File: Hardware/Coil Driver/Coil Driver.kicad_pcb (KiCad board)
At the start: 4 copper layers, 50 x 50 mm, 88 parts, among them J1 Barrel_Jack_Switch, J2 0.1" Header, J3 Tag-connect-NL, J4 0.1" Header, Q1 DMN3023L, Q2 DMN3023L, Q3 DMN3023L, Q4 DMN3023L, SW1 BTN_RST, SW2 BTN_USR1, SW3 BTN_USR2, U1 DGD05473, U2 MCP16331, U3 DGD05473, U4 STM32F070F6P6, Y1 8MHz

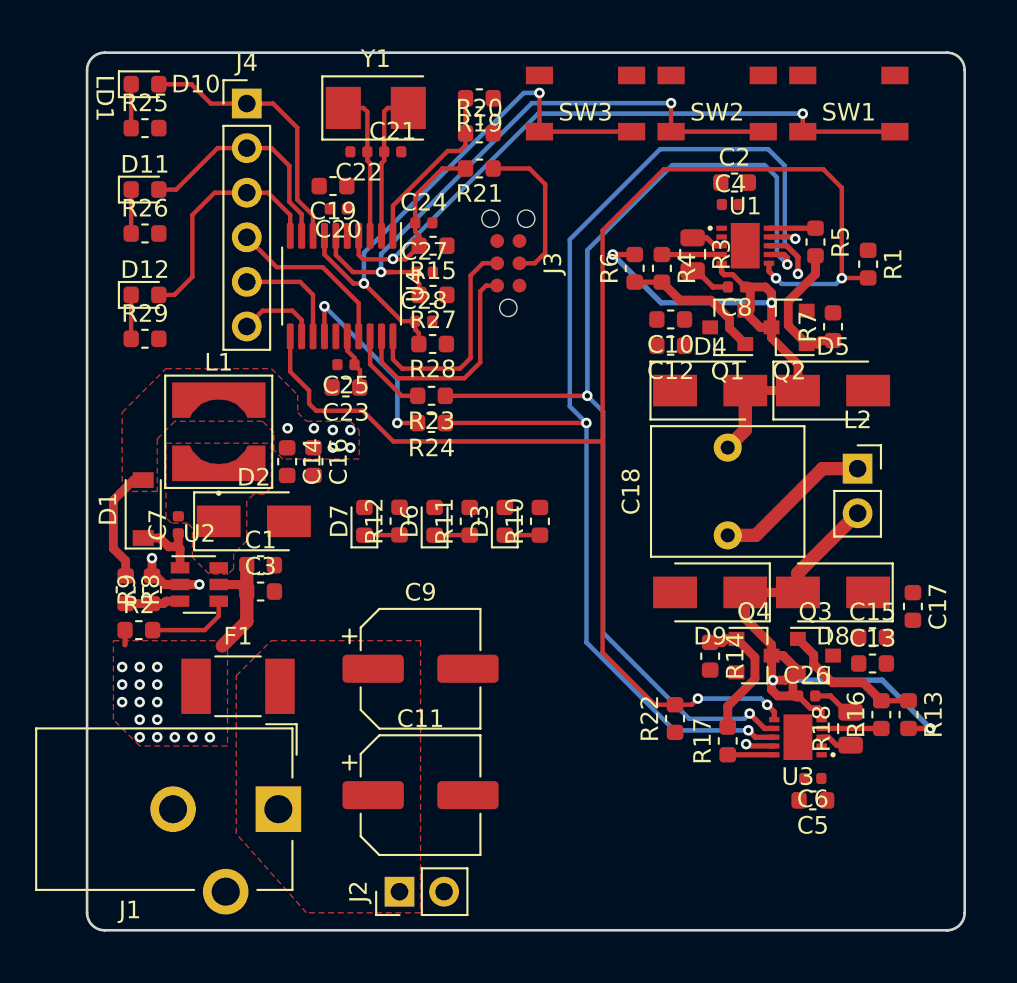
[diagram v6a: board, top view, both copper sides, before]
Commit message: added ground vias
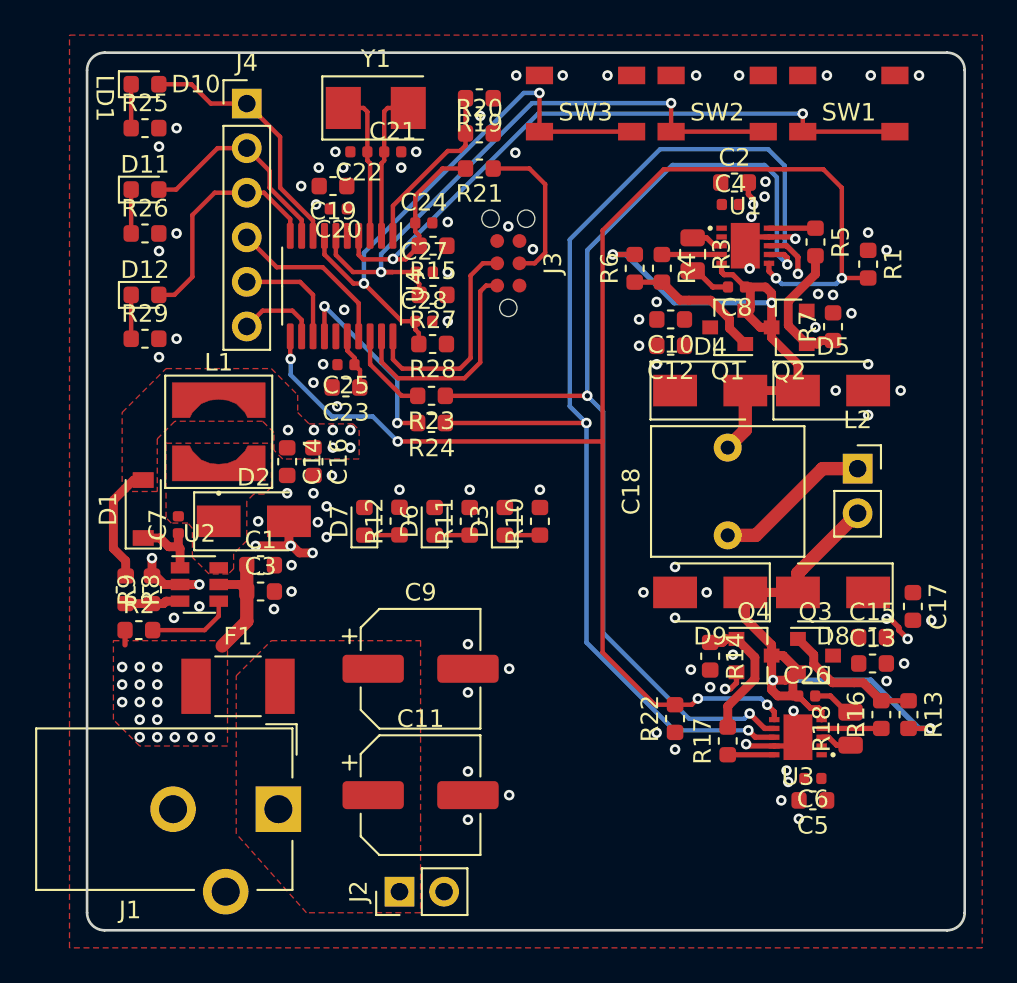
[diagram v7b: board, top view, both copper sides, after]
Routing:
- net GND: track 7.10 -> 19.6 mm, vias 4 -> 99
- net /LD1: track 15.4 -> 14.6 mm
- net /LD2: track 13.1 -> 12.3 mm
- net /GD_EN: track 86.5 -> 86.1 mm, vias 4 -> 6
- added copper zone on F.Cu, net GND

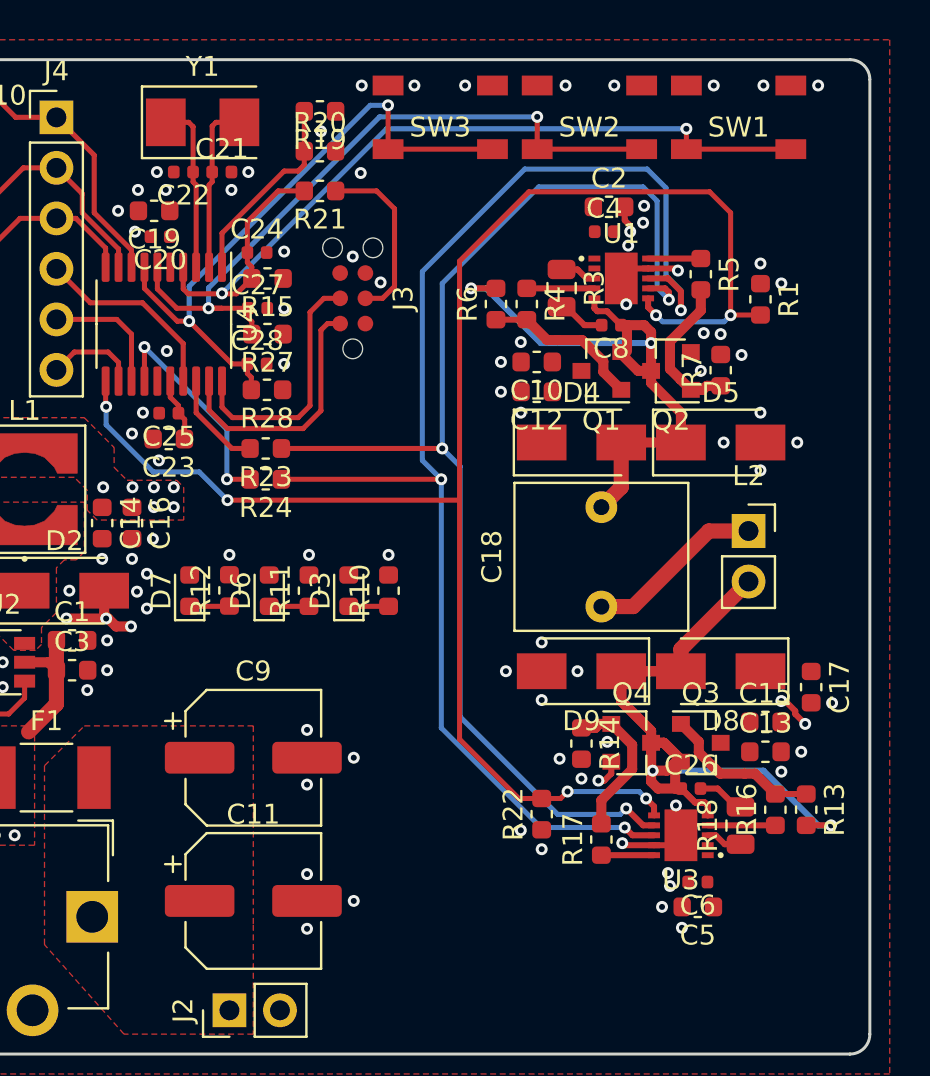
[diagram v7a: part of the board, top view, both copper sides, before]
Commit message: Added 12V and 3.3V vias, full connectivity. Passes DRC.
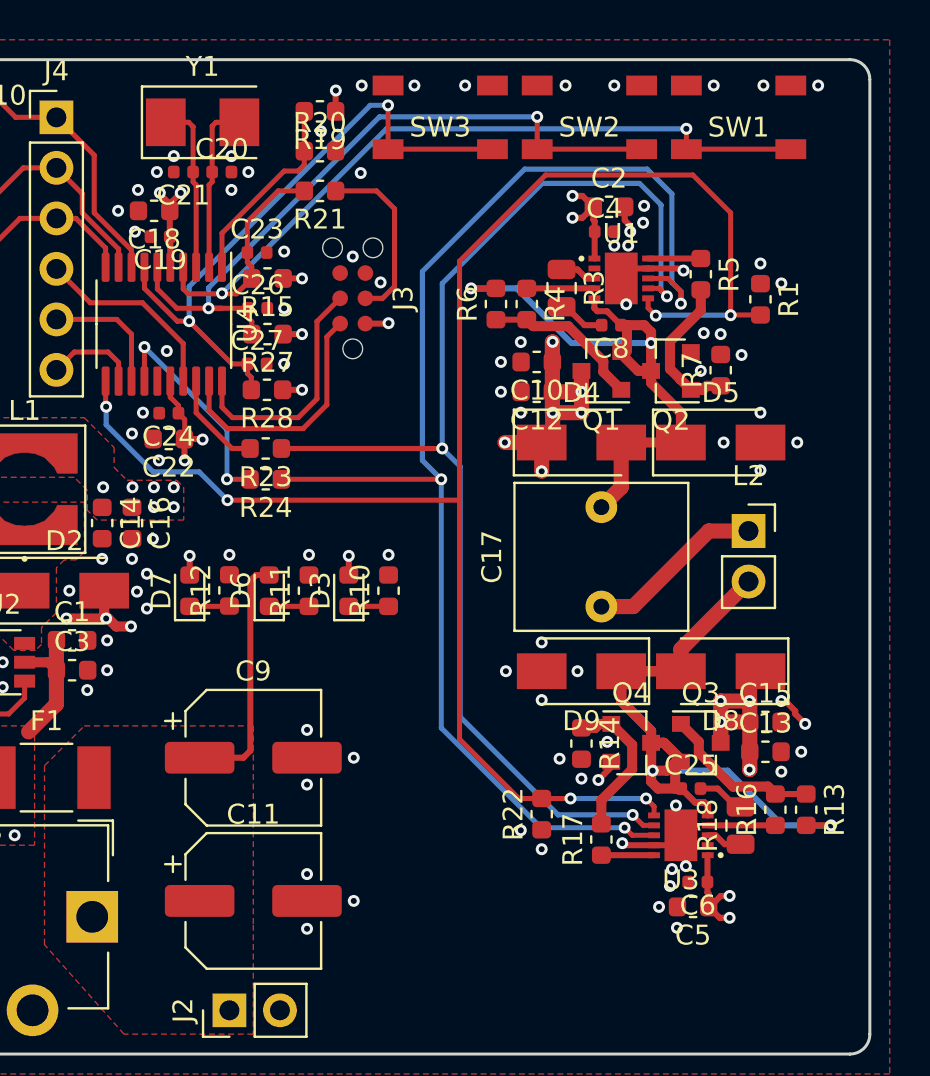
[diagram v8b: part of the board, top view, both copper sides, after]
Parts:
- removed the C17 at (173.1, 104.5)
- moved C5 0.24 mm to (167.1, 115.6)
- renumbered C18 to C17, C19 to C18, C20 to C19, C21 to C20, C22 to C21, C23 to C22, C24 to C23, C25 to C24, C26 to C25, C27 to C26, C28 to C27
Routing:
- net +12V: track 7.78 -> 44.5 mm, vias 16 -> 31
- net +3V3: track 10.00 -> 22.8 mm, vias 6 -> 16
- net VDD: track 0.00 -> 12.3 mm
- net /HIN: track 62.3 -> 61.6 mm
- net /LIN: track 68.4 -> 67.8 mm
- net GND: track 19.6 -> 19.7 mm, vias 99 -> 101
